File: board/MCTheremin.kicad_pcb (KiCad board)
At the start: 2 copper layers, 100 x 100 mm, 92 parts, among them J1 Barrel_Jack, J10 Conn_01x02, J11 Conn_01x01, J12 Conn_01x01, J13 Conn_01x01, J14 Conn_01x01, J15 Conn_01x01, J16 Conn_01x01, J17 Conn_01x02, J18 Conn_01x01, J19 Conn_01x04, J2 Conn_01x02, J20 Conn_01x04, J21 Conn_01x02, J22 Conn_01x02, J3 Conn_01x01, J4 Conn_01x01, J5 Conn_01x02, J6 Conn_01x02, J7 Conn_01x01, J8 Conn_01x01, J9 Conn_01x01, Q1 2N3904, Q2 2N3904, Q3 2N3904, SW1 SW_Push, SW2 SW_Push, U1 74HC04, U2 MCP4921, U3 LM7805_TO220, U4 LM386, U5 LM358, U6 74HC04

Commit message: Pre LC
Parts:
- added R25: 1k, Resistors_THT:R_Axial_DIN0207_L6.3mm_D2.5mm_P7.62mm_Horizontal, F.Cu at (120.9, 110.6)
- R10: value 10k -> 220R
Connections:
- U5 pad 6: Net-(C13-Pad1) -> Net-(R25-Pad1)
- U5 pad 7: Net-(C13-Pad1) -> Net-(R25-Pad1)
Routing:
- net Net-(R25-Pad1): track 0.00 -> 11.1 mm
- net Net-(C13-Pad1): track 26.7 -> 21.9 mm
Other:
- board text added: "LM7805"

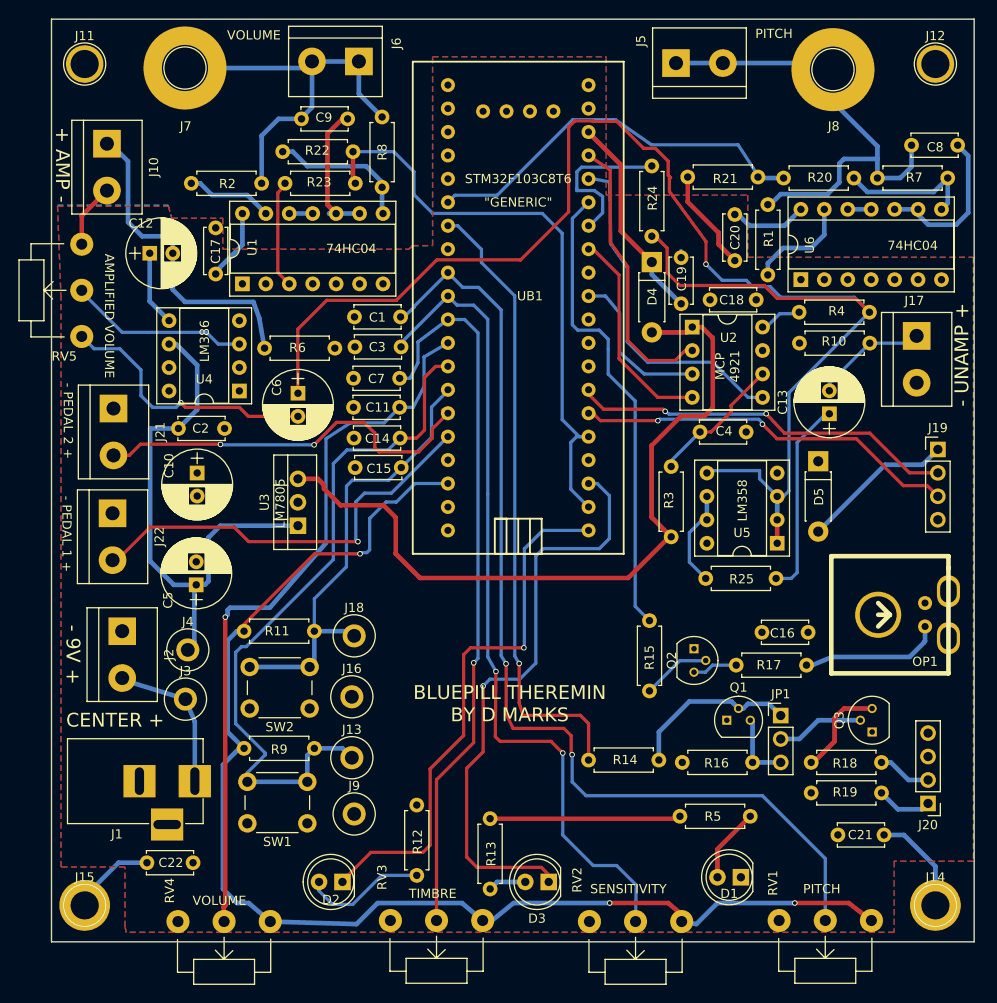
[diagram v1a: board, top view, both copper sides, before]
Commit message: Changed to LC oscillator - removed copper fill from under oscillator
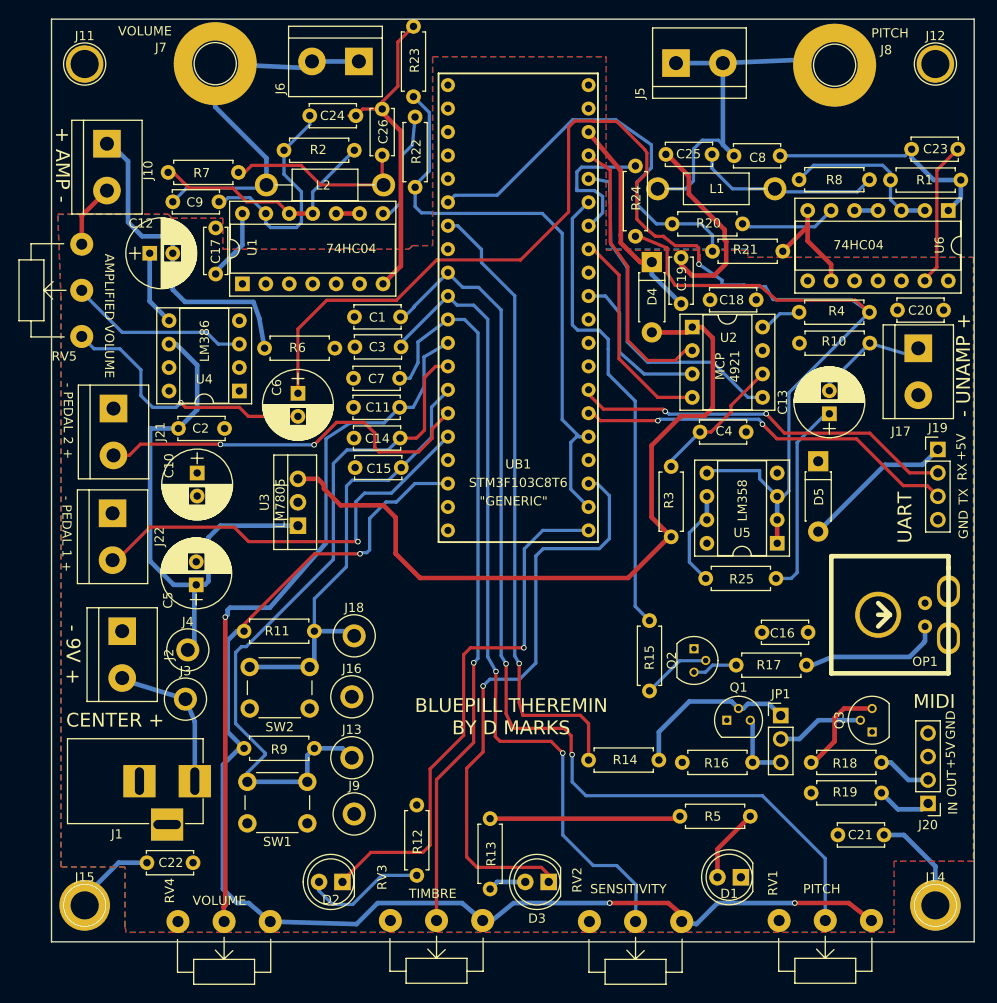
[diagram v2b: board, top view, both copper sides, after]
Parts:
- added C23: 100 pF, Capacitors_THT:C_Disc_D5.0mm_W2.5mm_P5.00mm, F.Cu at (143.2, 64.1)
- added C24: 100 pF, Capacitors_THT:C_Disc_D5.0mm_W2.5mm_P5.00mm, F.Cu at (78.0, 60.5)
- added C25: 220 pF, Capacitors_THT:C_Disc_D5.0mm_W2.5mm_P5.00mm, F.Cu at (116.6, 64.7)
- added C26: 220 pF, Capacitors_THT:C_Disc_D5.0mm_W2.5mm_P5.00mm, F.Cu at (85.8, 59.7)
- added L1: 1 mH, Inductors_THT:L_Axial_L7.0mm_D3.3mm_P12.70mm_Horizontal_Fastron_MICC, F.Cu at (128.4, 68.4)
- added L2: 1 mH, Inductors_THT:L_Axial_L7.0mm_D3.3mm_P12.70mm_Horizontal_Fastron_MICC, F.Cu at (86.0, 68.0)
- C8: value 33 pF -> 100 pF
- C9: value 47 pF -> 100 pF
- R1, R2: value 10k -> 2.2M
- R7, R8: value 10k -> 220R
- moved R7 84.5 mm to (62.6, 66.6), turned to 0 degrees
- moved R8 45.2 mm to (131.0, 67.4), turned to 0 degrees
- moved C20 24.9 mm to (146.7, 81.5), turned to 180 degrees
- moved C8 19.3 mm to (129.0, 64.8)
- moved R2 18.0 mm to (82.8, 64.2), turned to 180 degrees
- moved U6 17.6 mm to (147.2, 70.7), turned to 270 degrees
- moved R1 16.8 mm to (140.9, 67.4), turned to 0 degrees
- moved C9 16.6 mm to (68.1, 69.8)
- moved R22 14.8 mm to (89.4, 60.6), turned to 270 degrees
- moved R20 13.1 mm to (124.9, 72.2)
- moved R23 11.3 mm to (89.2, 58.4), turned to 90 degrees
- moved R21 9.44 mm to (121.6, 75.2), turned to 0 degrees
- moved J7 3.31 mm to (67.7, 54.8)
- moved R24 1.78 mm to (113.3, 65.9)
- moved J17 1.36 mm to (143.9, 85.7)
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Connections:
- C8 pad 1: Net-(C8-Pad1) -> Net-(C23-Pad1)
- C9 pad 1: Net-(C9-Pad1) -> Net-(C24-Pad1)
- R1 pad 2: Net-(C8-Pad2) -> Net-(C23-Pad1)
- R2 pad 2: Net-(C9-Pad2) -> Net-(C24-Pad1)
- R7 pad 1: Net-(R20-Pad1) -> Net-(R2-Pad1)
- R7 pad 2: Net-(C8-Pad2) -> Net-(C26-Pad2)
- R8 pad 1: Net-(R22-Pad1) -> Net-(R1-Pad1)
- R8 pad 2: Net-(C9-Pad2) -> Net-(C25-Pad2)
- U1 pad 10: Net-(C9-Pad1) -> Net-(U1-Pad10)
- U1 pad 11: Net-(U1-Pad11) -> Net-(R2-Pad1)
- U1 pad 12: Net-(U1-Pad11) -> Net-(R2-Pad1)
- U1 pad 13: Net-(R2-Pad1) -> Net-(C24-Pad1)
- U1 pad 9: Net-(C9-Pad1) -> Net-(U1-Pad10)
- U6 pad 1: GND -> Net-(C23-Pad1)
- U6 pad 10: Net-(C8-Pad1) -> (no net)
- U6 pad 11: Net-(U6-Pad11) -> GND
- U6 pad 12: Net-(U6-Pad11) -> (no net)
- U6 pad 13: Net-(R1-Pad1) -> GND
- U6 pad 2: (no net) -> Net-(R1-Pad1)
- U6 pad 3: GND -> Net-(R1-Pad1)
- U6 pad 4: (no net) -> Net-(U6-Pad4)
- U6 pad 5: GND -> Net-(U6-Pad4)
- U6 pad 6: (no net) -> Net-(R20-Pad1)
- U6 pad 8: Net-(R20-Pad1) -> (no net)
- U6 pad 9: Net-(C8-Pad1) -> GND
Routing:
- net GND: track 31.1 -> 93.7 mm
- net Net-(C23-Pad1): track 0.00 -> 25.7 mm
- net Net-(C24-Pad1): track 0.00 -> 24.8 mm
- net Net-(C26-Pad2): track 0.00 -> 20.2 mm
- net Net-(C25-Pad2): track 0.00 -> 20.2 mm
- net Net-(C8-Pad1): track 17.3 -> 0.00 mm
- net Net-(R2-Pad1): track 9.43 -> 26.2 mm
- net Net-(C9-Pad1): track 16.0 -> 0.00 mm
- net +5V: track 120.1 -> 111.7 mm
- net Net-(C8-Pad2): track 55.0 -> 47.0 mm
- net Net-(R1-Pad1): track 11.4 -> 18.0 mm
- net Net-(C6-Pad1): track 163.8 -> 168.9 mm
- net Net-(R20-Pad1): track 15.1 -> 10.5 mm
- net Net-(R22-Pad1): track 15.6 -> 12.4 mm
- net Net-(U6-Pad4): track 0.00 -> 2.54 mm
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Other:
- board text added: "+5V"
- board text added: "GND"
- board text added: "IN"
- board text added: "MIDI"
- board text added: "OUT"
- board text added: "RX"
- board text added: "TX"
- board text added: "UART"

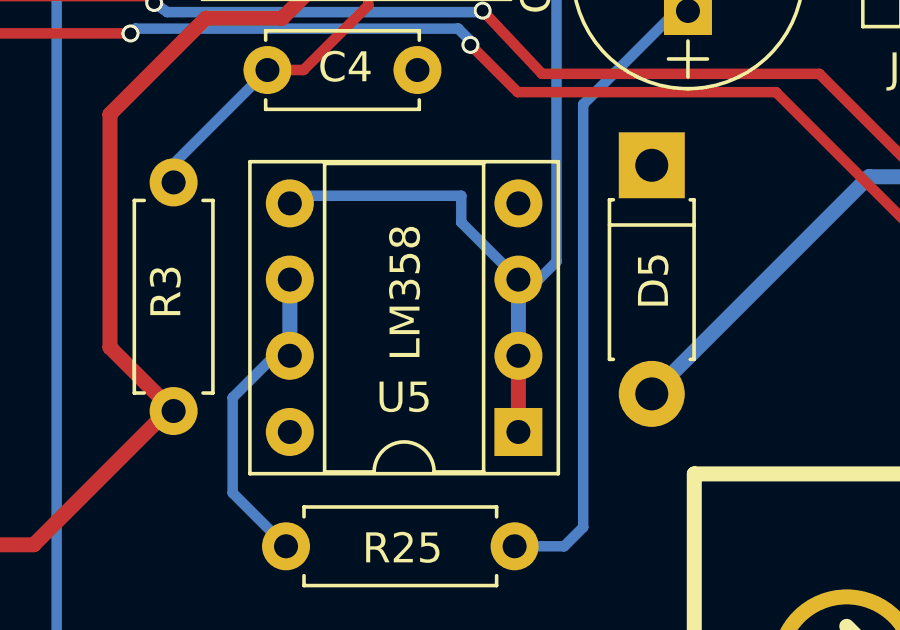
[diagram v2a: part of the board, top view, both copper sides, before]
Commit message: Accidental connection in LM358
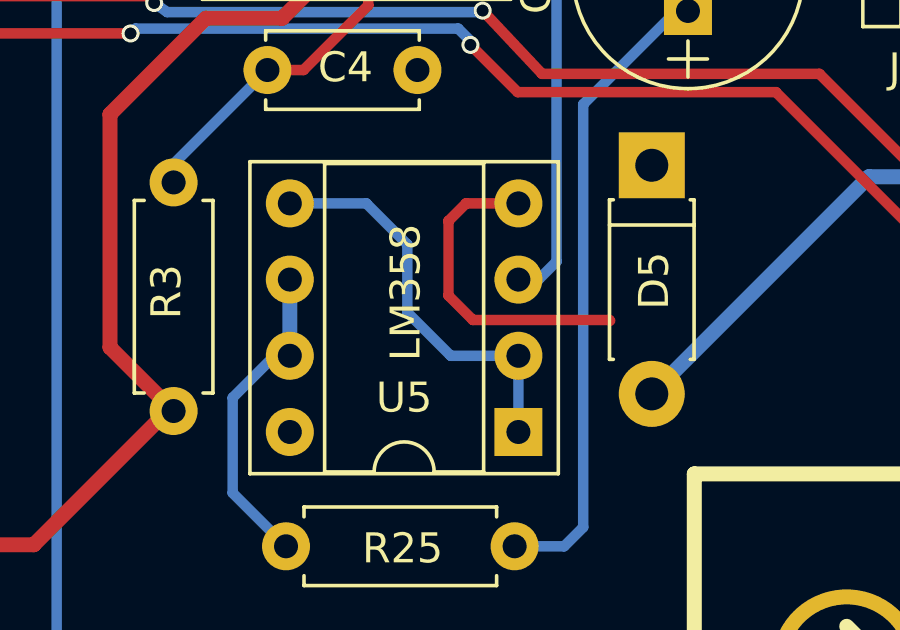
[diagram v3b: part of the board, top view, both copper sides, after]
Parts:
- C23: value 100 pF -> 150 pF
- C24: value 100 pF -> 220 pF
- C25: value 220 pF -> 150 pF
- L1, L2: value 1 mH -> 400 uH
- R25: value 1k -> 220R
- R7, R8: value 220R -> 1k
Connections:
- U5 pad 1: Net-(C6-Pad1) -> Net-(U5-Pad1)
- U5 pad 2: Net-(C6-Pad1) -> Net-(U5-Pad1)
- U5 pad 5: Net-(C6-Pad1) -> Net-(U5-Pad1)
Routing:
- net Net-(C6-Pad1): track 168.9 -> 154.3 mm
- net Net-(U5-Pad1): track 0.00 -> 14.1 mm
- net GND: track 93.7 -> 104.5 mm
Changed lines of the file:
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@@
 (kicad_pcb (version 4) (host pcbnew 4.0.7)
   (general
-    (links 195)
+    (links 194)
     (no_connects 0)
-    (area 49.924999 49.924999 150.075001 150.075001)
+    (area 46.001499 48.5296 150.81032 155.077601)
     (thickness 1.6)
     (drawings 34)
-    (tracks 680)
+    (tracks 687)
     (zones 0)
     (modules 99)
-    (nets 65)
+    (nets 66)
   )
   (page A4)
@@
   (net 63 "Net-(U1-Pad10)")
   (net 64 "Net-(U6-Pad4)")
+  (net 65 "Net-(U5-Pad1)")
   (net_class Default "This is the default net class."
     (clearance 0.2)
@@
     (add_net "Net-(RV5-Pad2)")
     (add_net "Net-(U1-Pad10)")
+    (add_net "Net-(U5-Pad1)")
     (add_net "Net-(U6-Pad4)")
     (add_net PITCH)
@@
     )
     (pad 1 thru_hole rect (at 0 0 180) (size 1.6 1.6) (drill 0.8) (layers *.Cu *.Mask)
-      (net 6 "Net-(C6-Pad1)"))
+      (net 65 "Net-(U5-Pad1)"))
     (pad 5 thru_hole oval (at 7.62 7.62 180) (size 1.6 1.6) (drill 0.8) (layers *.Cu *.Mask)
-      (net 6 "Net-(C6-Pad1)"))
+      (net 65 "Net-(U5-Pad1)"))
     (pad 2 thru_hole oval (at 0 2.54 180) (size 1.6 1.6) (drill 0.8) (layers *.Cu *.Mask)
-      (net 6 "Net-(C6-Pad1)"))
+      (net 65 "Net-(U5-Pad1)"))
     (pad 6 thru_hole oval (at 7.62 5.08 180) (size 1.6 1.6) (drill 0.8) (layers *.Cu *.Mask)
       (net 58 "Net-(R25-Pad1)"))
@@
       (effects (font (size 1 1) (thickness 0.15)))
     )
-    (fp_text value 220R (at 3.81 2.31) (layer F.Fab)
+    (fp_text value 1k (at 3.81 2.31) (layer F.Fab)
       (effects (font (size 1 1) (thickness 0.15)))
     )
@@
       (effects (font (size 1 1) (thickness 0.15)))
     )
-    (fp_text value 220R (at 3.81 2.31) (layer F.Fab)
+    (fp_text value 1k (at 3.81 2.31) (layer F.Fab)
       (effects (font (size 1 1) (thickness 0.15)))
     )
@@
       (effects (font (size 1 1) (thickness 0.15)))
     )
-    (fp_text value 1k (at 3.81 2.31) (layer F.Fab)
+    (fp_text value 220R (at 3.81 2.31) (layer F.Fab)
       (effects (font (size 1 1) (thickness 0.15)))
     )
@@
       (effects (font (size 1 1) (thickness 0.15)))
     )
-    (fp_text value "100 pF" (at 2.5 2.56) (layer F.Fab)
+    (fp_text value "150 pF" (at 2.5 2.56) (layer F.Fab)
       (effects (font (size 1 1) (thickness 0.15)))
     )
@@
       (effects (font (size 1 1) (thickness 0.15)))
     )
-    (fp_text value "100 pF" (at 2.5 2.56) (layer F.Fab)
+    (fp_text value "220 pF" (at 2.5 2.56) (layer F.Fab)
       (effects (font (size 1 1) (thickness 0.15)))
     )
@@
       (effects (font (size 1 1) (thickness 0.15)))
     )
-    (fp_text value "220 pF" (at 2.5 2.56) (layer F.Fab)
+    (fp_text value "150 pF" (at 2.5 2.56) (layer F.Fab)
       (effects (font (size 1 1) (thickness 0.15)))
     )
@@
       (effects (font (size 1 1) (thickness 0.15)))
     )
-    (fp_text value "1 mH" (at 6.35 2.71 180) (layer F.Fab)
+    (fp_text value "400 uH" (at 6.35 2.71 180) (layer F.Fab)
       (effects (font (size 1 1) (thickness 0.15)))
     )
@@
       (effects (font (size 1 1) (thickness 0.15)))
     )
-    (fp_text value "1 mH" (at 6.35 2.71 180) (layer F.Fab)
+    (fp_text value "400 uH" (at 6.35 2.71 180) (layer F.Fab)
       (effects (font (size 1 1) (thickness 0.15)))
     )
@@
   (segment (start 98.298 69.088) (end 93.726 69.088) (width 0.35) (layer B.Cu) (net 1))
   (segment (start 92.964 69.85) (end 93.726 69.088) (width 0.35) (layer B.Cu) (net 1) (status 20))
+  (segment (start 128.651 99.187) (end 126.90348 99.187) (width 0.35) (layer F.Cu) (net 2))
+  (segment (start 131.68376 103.0732) (end 131.70916 103.0986) (width 0.35) (layer F.Cu) (net 2))
+  (segment (start 127.13208 103.0732) (end 131.68376 103.0732) (width 0.35) (layer F.Cu) (net 2))
+  (segment (start 126.31928 102.2604) (end 127.13208 103.0732) (width 0.35) (layer F.Cu) (net 2))
+  (segment (start 126.31928 99.7712) (end 126.31928 102.2604) (width 0.35) (layer F.Cu) (net 2))
+  (segment (start 126.90348 99.187) (end 126.31928 99.7712) (width 0.35) (layer F.Cu) (net 2))
   (segment (start 85.8393 59.7408) (end 85.8393 60.10656) (width 0.5) (layer F.Cu) (net 2))
   (segment (start 85.8393 60.10656) (end 87.8713 62.13856) (width 0.5) (layer F.Cu) (net 2))
@@
   (segment (start 120.1674 75.565) (end 120.1674 76.073) (width 0.35) (layer F.Cu) (net 6))
   (segment (start 120.142 75.565) (end 120.1674 75.565) (width 0.35) (layer F.Cu) (net 6))
-  (segment (start 128.651 104.267) (end 128.651 106.807) (width 0.5) (layer F.Cu) (net 6))
   (segment (start 114.3 64.135) (end 111.252 61.087) (width 0.35) (layer F.Cu) (net 6))
   (segment (start 108.712 61.087) (end 108.712 61.0362) (width 0.35) (layer F.Cu) (net 6))
@@
   (segment (start 128.5875 80.4545) (end 137.0838 80.4545) (width 0.35) (layer F.Cu) (net 6))
   (segment (start 137.0838 80.4545) (end 138.6459 81.7626) (width 0.35) (layer F.Cu) (net 6))
-  (segment (start 126.746 98.933) (end 121.285 98.933) (width 0.35) (layer B.Cu) (net 6) (status 20))
-  (segment (start 121.285 98.933) (end 121.031 99.187) (width 0.35) (layer B.Cu) (net 6) (status 30))
-  (segment (start 126.746 99.822) (end 128.651 101.727) (width 0.35) (layer B.Cu) (net 6) (status 20))
-  (segment (start 126.746 98.933) (end 126.746 99.822) (width 0.35) (layer B.Cu) (net 6))
-  (segment (start 128.651 104.267) (end 128.651 101.727) (width 0.5) (layer B.Cu) (net 6) (status 30))
-  (segment (start 121.1072 99.2632) (end 121.031 99.187) (width 0.5) (layer B.Cu) (net 6) (status 30))
   (segment (start 138.684 85.1154) (end 143.1544 86.4616) (width 0.35) (layer B.Cu) (net 7) (status 20))
   (segment (start 143.1544 86.4616) (end 143.9418 85.6742) (width 0.35) (layer B.Cu) (net 7) (status 30))
@@
   (segment (start 80.8482 71.0692) (end 83.3882 71.0692) (width 0.5) (layer F.Cu) (net 63))
   (segment (start 139.573 70.739) (end 137.033 70.739) (width 0.5) (layer B.Cu) (net 64))
+  (segment (start 121.031 99.187) (end 123.58116 99.187) (width 0.35) (layer B.Cu) (net 65))
+  (segment (start 126.39548 104.267) (end 128.651 104.267) (width 0.35) (layer B.Cu) (net 65))
+  (segment (start 124.94768 102.8192) (end 126.39548 104.267) (width 0.35) (layer B.Cu) (net 65))
+  (segment (start 124.94768 100.55352) (end 124.94768 102.8192) (width 0.35) (layer B.Cu) (net 65))
+  (segment (start 123.58116 99.187) (end 124.94768 100.55352) (width 0.35) (layer B.Cu) (net 65))
+  (segment (start 128.651 106.807) (end 128.651 104.267) (width 0.35) (layer B.Cu) (net 65))
+  (segment (start 121.285 98.933) (end 121.031 99.187) (width 0.35) (layer B.Cu) (net 65) (status 30))
+  (segment (start 121.1072 99.2632) (end 121.031 99.187) (width 0.5) (layer B.Cu) (net 65) (status 30))
   (zone (net 2) (net_name GND) (layer F.Cu) (hatch edge 0.508)
     (connect_pads (clearance 0.5))
